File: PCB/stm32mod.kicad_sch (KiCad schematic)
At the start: 36 parts, among them J1 Debug, U42 AMS1117-3.3, U44 TYPE-C-31-M-12, U48 USBLC6-2SC6, X1 Crystal

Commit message: Ready to work on PCB
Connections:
- net GND: now also C1.1, C2.1, U44.0 (SH)
- no-connect marks 6 -> 2
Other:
- moved on the sheet: R12

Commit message: Plugin works.
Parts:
- renumbered C1 to C55001, C2 to C55002, C13 to C55013, C14 to C55014, LEDC1 to CL11, D2 to D55001, D7 to D55002, D6 to D55003, D1 to D55004, J1 to J55001, PB1 to PB55001, PB2 to PB55002, R1 to R55001, R5 to R55002, R2 to R55003, R3 to R55004, R10 to R55005, R9 to R55006, R4 to R55007, R12 to R55008, R11 to R55009, R13 to R55010, STM1 to STM55001, U42 to U55001, U44 to U55002, U48 to U55003, X1 to X55001

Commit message: Laying out the PCB.
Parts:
- removed CL11 (x6): 100nF, Capacitor_SMD:C_0402_1005Metric, symbol JLCPCB:CL05B104KO5NNNC
- removed CL11: 1uF, Capacitor_SMD:C_0402_1005Metric, symbol JLCPCB:CL05B104KO5NNNC
- removed CL11: 10nF, Capacitor_SMD:C_0402_1005Metric, symbol JLCPCB:CL05B104KO5NNNC
- removed CL11: 4.7uF, Capacitor_SMD:C_0603_1608Metric, symbol JLCPCB:CL05B104KO5NNNC
- removed PB55002: TS-1187A-B-A-B, footprint:SW-SMD_4P-L5.1-W5.1-P3.70-LS6.5-TL-2, symbol JLCPCB:TS-1187A-B-A-B
- removed R55005: 5.1k, Resistor_SMD:R_0402_1005Metric, symbol Device:R
- added PB52001: TS-1187A-B-A-B, footprint:SW-SMD_4P-L5.1-W5.1-P3.70-LS6.5-TL-2, symbol JLCPCB:TS-1187A-B-A-B
- R55006: value 5.1k -> 7.7k; LCSC C25905 -> C25918
- renumbered CL11 to CL24
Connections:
- net +5V: now also R55006.1
- net BOOT0: now also PB55001.3 (C), PB55001.4 (D)
- net GND: now also PB52001.2 (B); no longer PB55001.3 (C), PB55001.4 (D)
- net NRST: now also PB52001.4 (D)
- net at CL24.2, R55004.2: now also PB52001.3 (C)
- net at CL24.1: now also PB52001.1 (A)
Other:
- note removed: "Input Voltage Decoupling"
- moved on the sheet: C55001, C55002, R55003

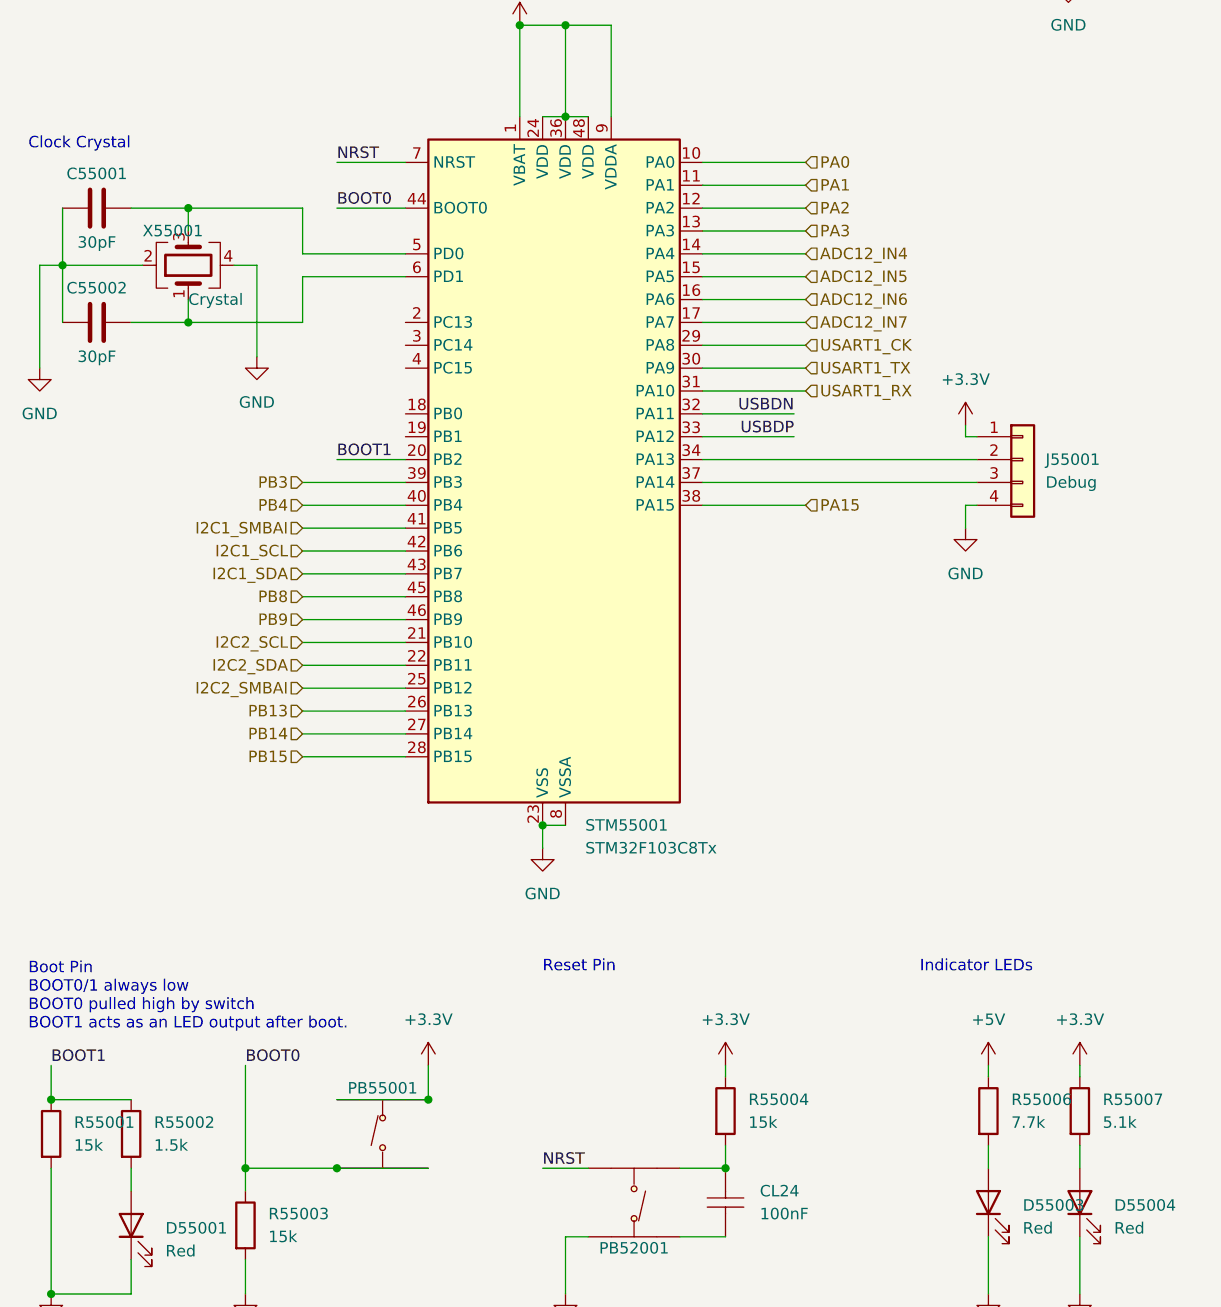
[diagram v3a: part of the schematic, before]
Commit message: Removed 8-key units, now using the PCB view to handle routing the keys to the SOIP shift registers.
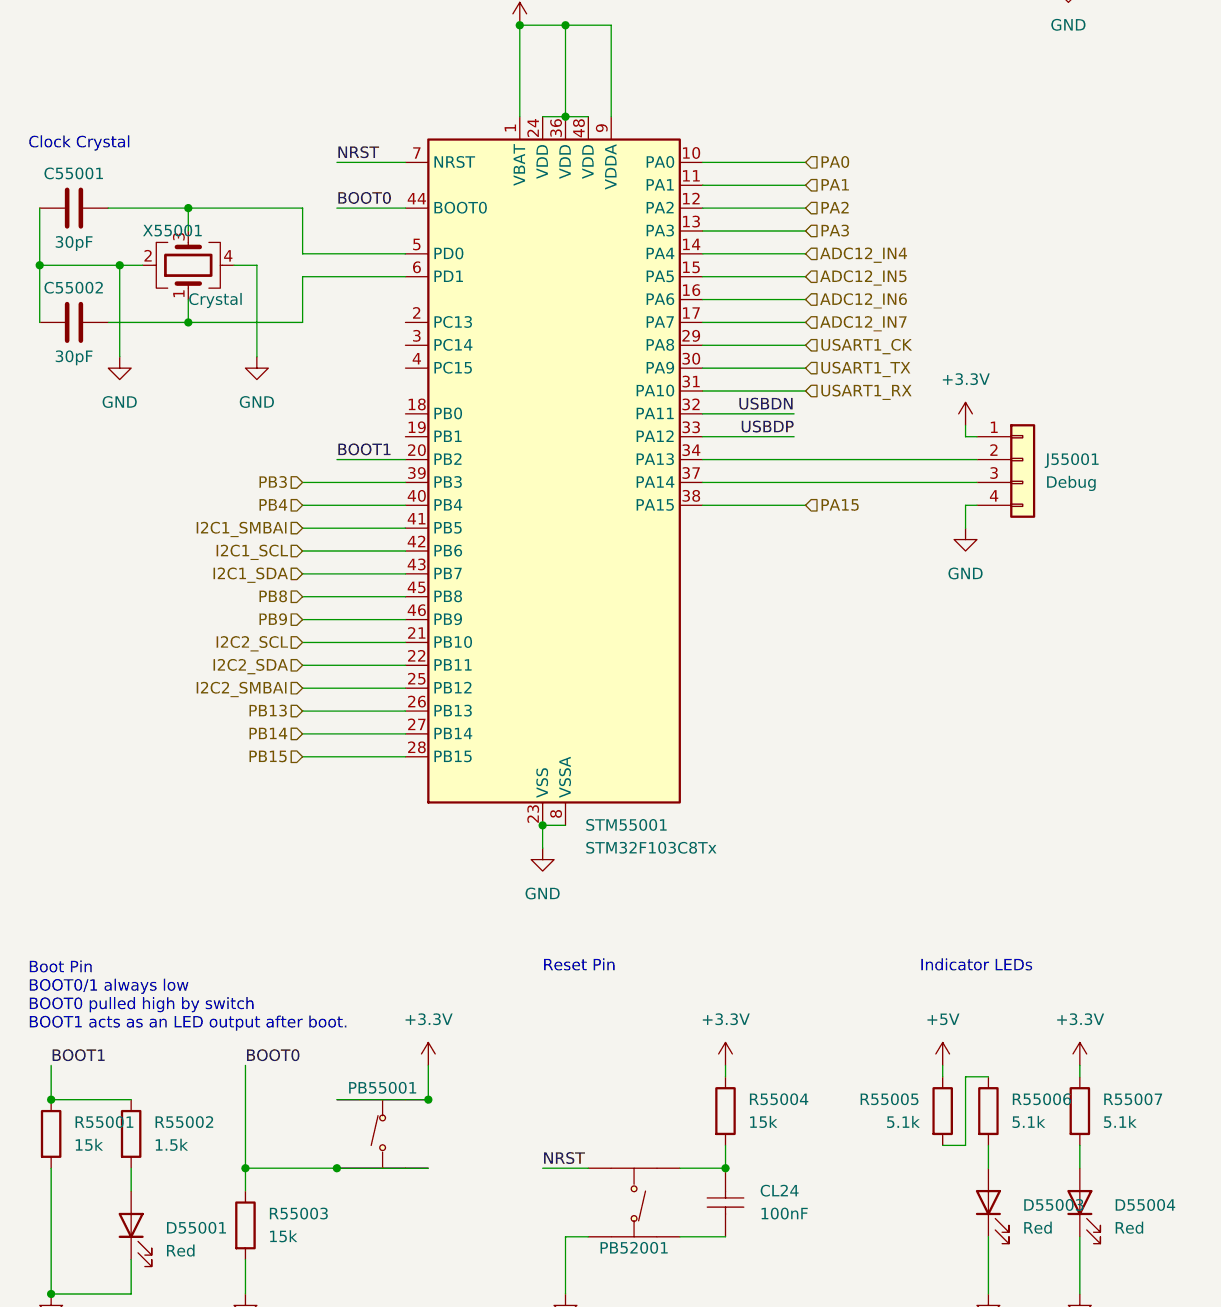
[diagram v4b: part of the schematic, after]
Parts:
- added R55005: 5.1k, Resistor_SMD:R_0402_1005Metric, symbol Device:R
- R55006: value 7.7k -> 5.1k; LCSC C25918 -> C25905
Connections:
- net +5V: now also R55005.1; no longer R55006.1
- new net: R55005.2, R55006.1
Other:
- moved on the sheet: C55001, C55002

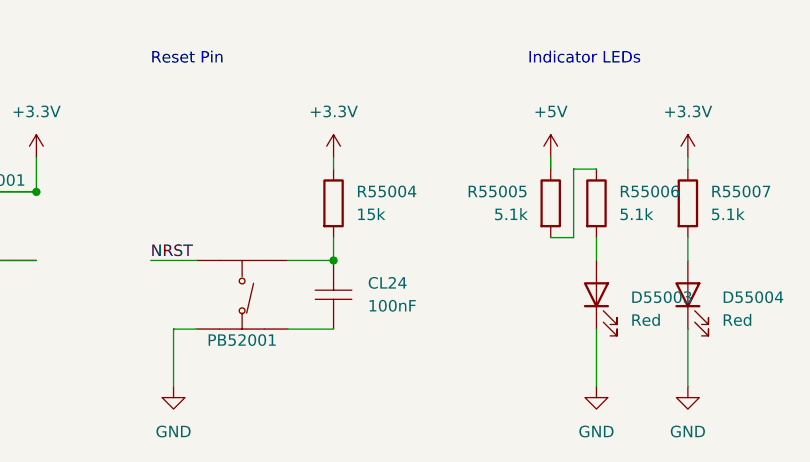
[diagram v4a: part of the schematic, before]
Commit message: Updated schematics for KiCAD 8
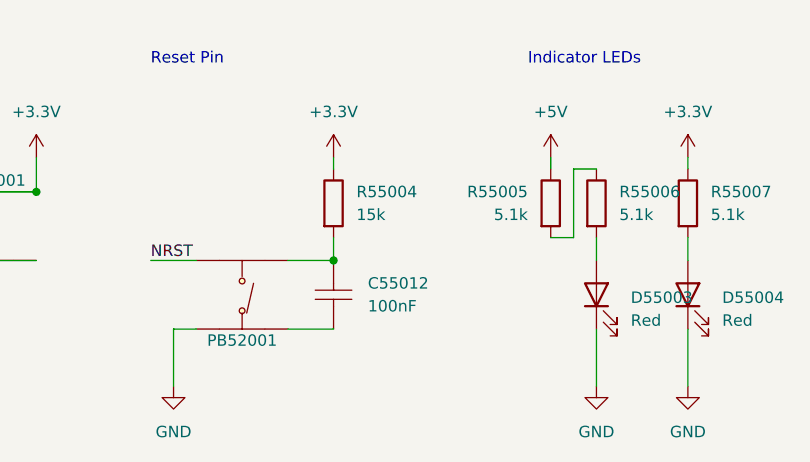
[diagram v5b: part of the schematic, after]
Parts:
- renumbered CL24 to C55012
